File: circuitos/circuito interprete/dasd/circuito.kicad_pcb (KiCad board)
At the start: 2 copper layers, 20 parts, among them IC1 ATMEGA328-P, P1 CONN_5V, P10 CONN_LIM_Y, P11 CONN_E_STOP, P2 CONN_02X03, P3 CONN_EJE_X, P4 CONN_EJE_Y, P5 CONN_EJE_Z, P6 CONN_HUS, P7 CONN_UART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

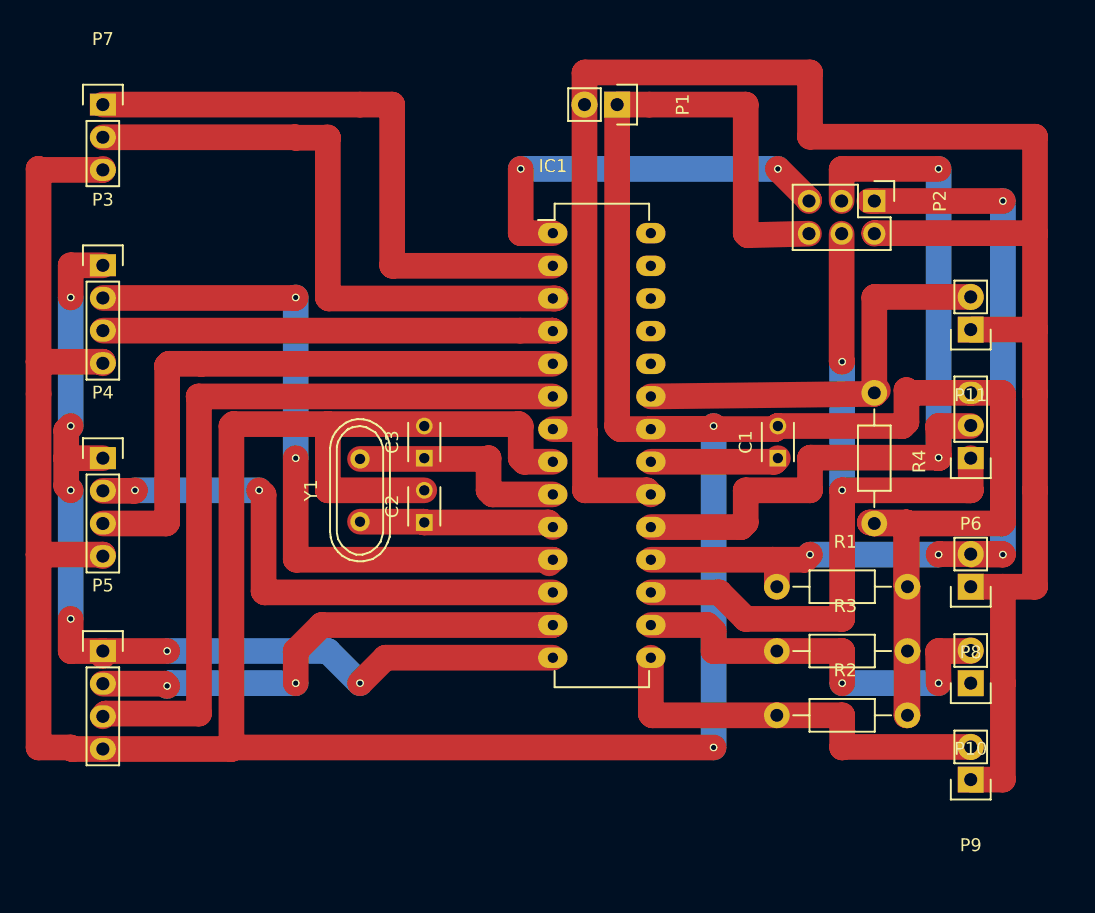
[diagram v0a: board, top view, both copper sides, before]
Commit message: agrego ruteo de placas
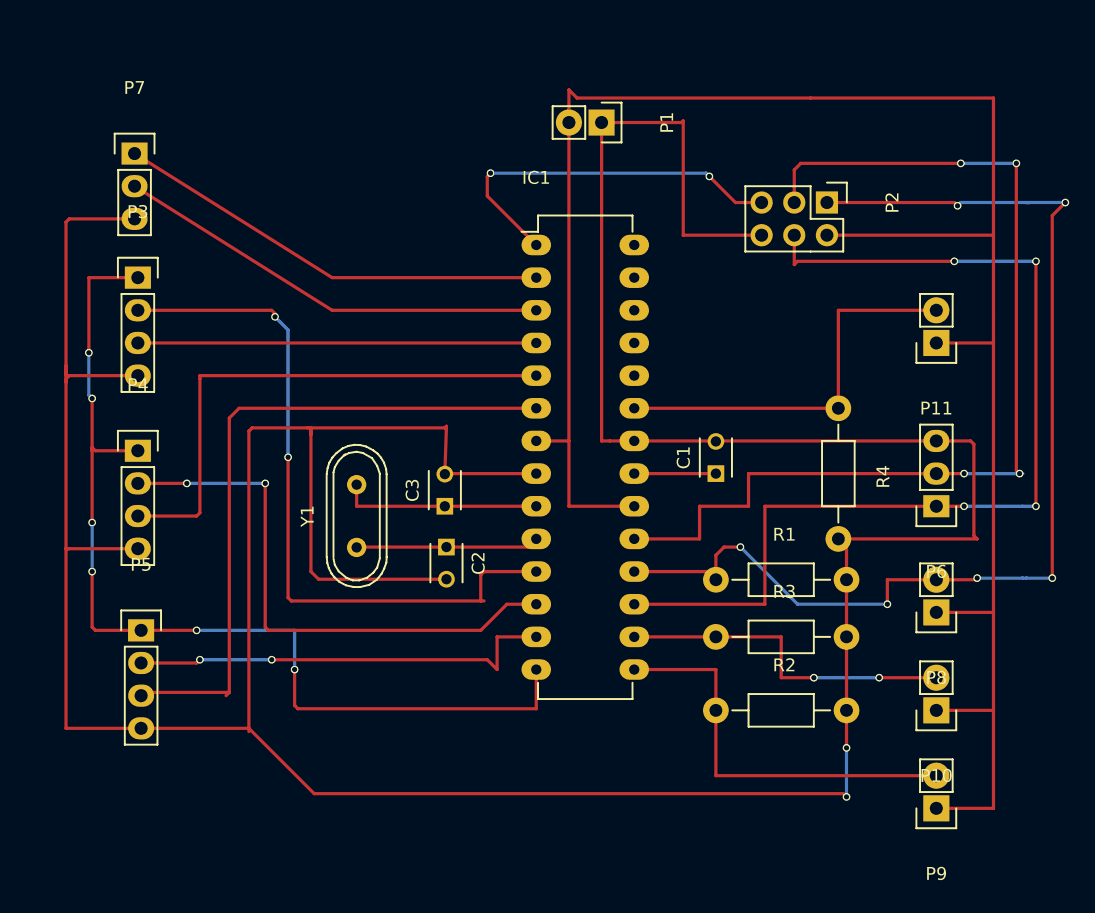
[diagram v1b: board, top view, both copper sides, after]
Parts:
- moved C1 4.97 mm to (170.2, 76.2)
- moved R3 4.87 mm to (175.3, 88.9)
- moved R1 4.77 mm to (175.3, 84.5)
- moved R2 4.76 mm to (175.3, 94.6)
- moved P6 4.60 mm to (187.3, 78.7)
- moved P7 4.54 mm to (125.0, 51.3)
- moved C3 4.07 mm to (149.1, 78.7)
- moved P2 3.69 mm to (178.8, 55.1)
- moved P9 3.49 mm to (187.3, 102.2)
- moved P10 3.41 mm to (187.3, 94.6)
- moved P5 3.38 mm to (125.5, 88.4)
- moved P8 3.34 mm to (187.3, 87.0)
- moved R4 3.04 mm to (179.7, 76.2)
- moved P3 2.89 mm to (125.2, 61.0)
- moved P11 2.87 mm to (187.3, 66.0)
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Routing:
- net GND: track 345.8 -> 306.5 mm
- net /step_X: track 65.1 -> 31.0 mm
- net /MOSI: track 58.6 -> 79.1 mm, vias 2 -> 4
- net /MISO: track 71.1 -> 87.4 mm, vias 4 -> 6
- net /SCK: track 65.1 -> 79.6 mm, vias 2 -> 4
- net /Tx_int: track 47.9 -> 34.0 mm
- net /Rx_int: track 47.5 -> 34.0 mm
- net /step_Z: track 60.1 -> 52.9 mm
- net /step_Y: track 47.5 -> 41.8 mm
- net /dir_Z: track 39.3 -> 33.7 mm
- net /lim_Y: track 31.6 -> 26.7 mm
- net Net-(C1-Pad1): track 10.00 -> 6.35 mm
- net VCC: track 155.7 -> 159.3 mm
- net /enable: track 75.4 -> 78.7 mm
- net /RESET: track 31.7 -> 29.3 mm
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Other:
- net class Default: clearance 0.15 -> 0.25; trace_width 2 -> 0.25
- rule trace_clearance: 0.15 -> 0.25
